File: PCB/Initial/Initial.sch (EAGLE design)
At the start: 52 parts, among them U2 AT24C512C-SHD-B

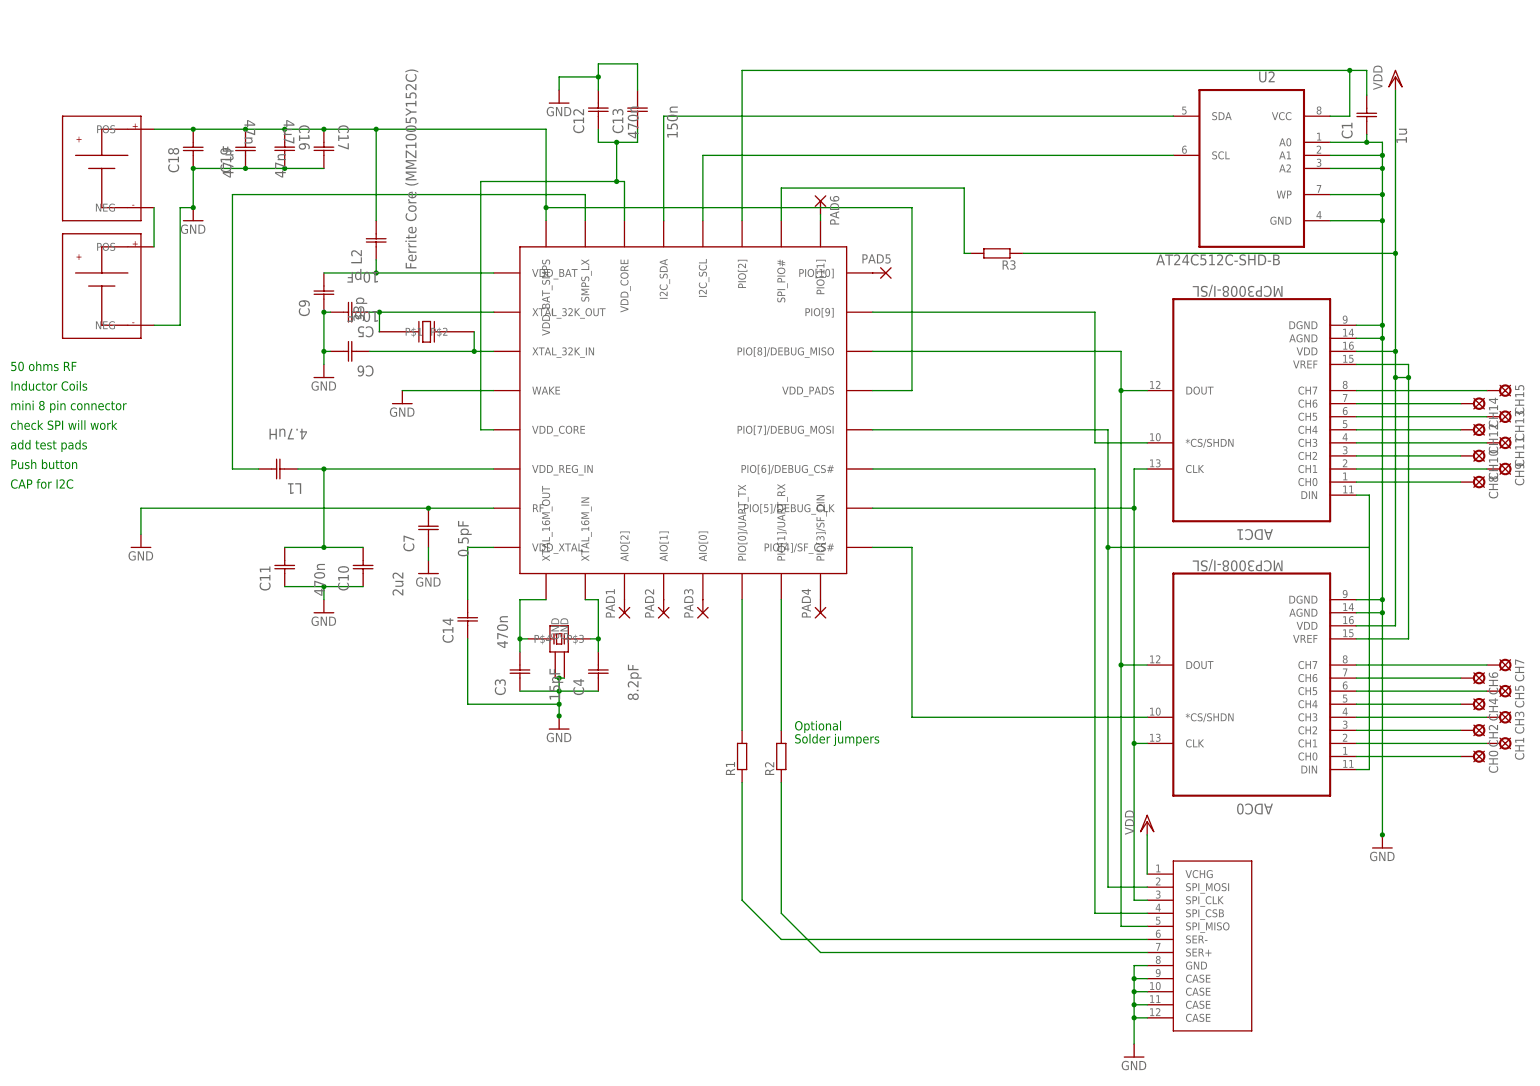
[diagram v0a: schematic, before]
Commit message: using project to link schem and board. Need RF still
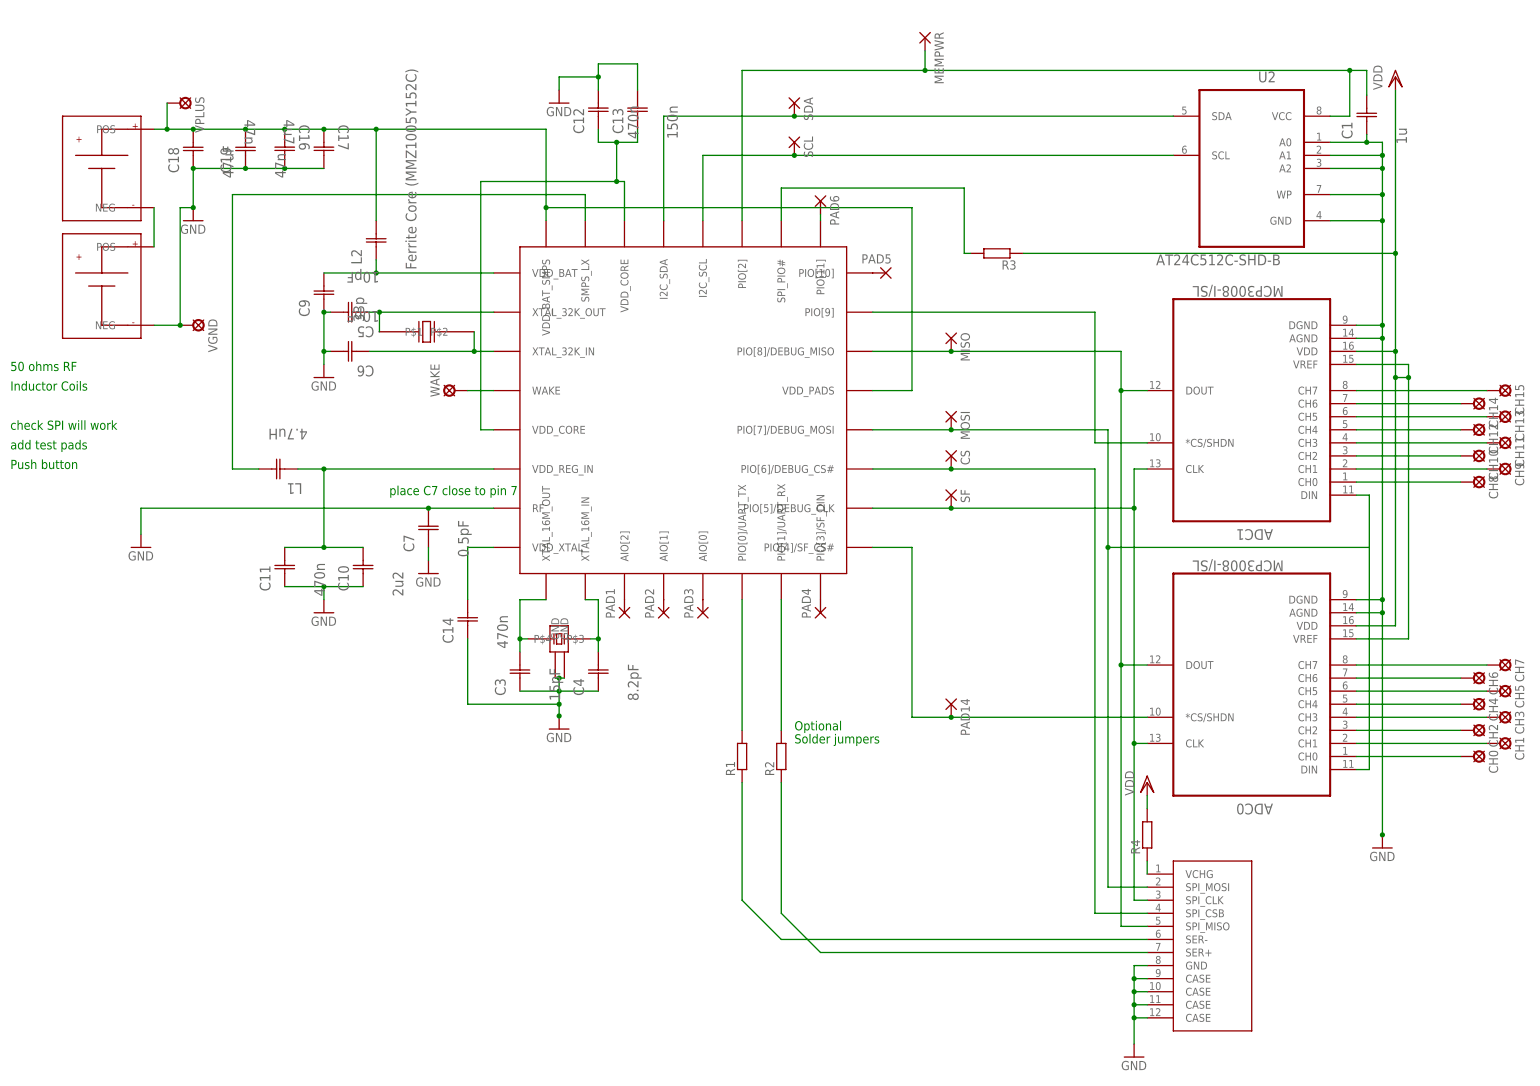
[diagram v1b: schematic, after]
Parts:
- added CS, MEMPWR, MISO, MOSI, PAD14, SCL, SDA, SF: (no value), wirepad:1,6/0,8
- added R4: (no value), resistor-shunt:BVS
- added VGND: LSP10, solpad:LSP10
- added VPLUS, WAKE: Vrail, solpad:LSP10
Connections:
- new net N$40: R4.2, U$2.VCHG
- new net N$49: U$1.WAKE, WAKE.MP
- net GND: now also VGND.MP; no longer U$1.WAKE
- net N$17: now also SDA.P
- net N$18: now also SCL.P
- net N$21: now also SF.P
- net N$22: now also MISO.P
- net N$23: now also MOSI.P
- net N$25: now also PAD14.P
- net N$31: now also CS.P
- net N$34: now also VPLUS.MP
- net N$46: now also MEMPWR.P
- net VDD: now also R4.1; no longer U$2.VCHG
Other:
- note added: "place C7 close to pin 7"
- note removed: "CAP for I2C"
- note removed: "mini 8 pin connector"
